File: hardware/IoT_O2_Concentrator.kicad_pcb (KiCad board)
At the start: 2 copper layers, 92.8 x 88.4 mm, 17 parts, among them J1 5V_SUPPLY_BUCK_OUT, J10 12V_SUPPLY_BUCK_IN, J11 O2_VCC_SELECTOR, J12 BOX_SWITCH, J13 AC-DC_MODULE, J2 BUZZER, J3 O2_SENSOR, J4 GPIOs, J5 RELAY, J6 LCD_20x04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

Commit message: Finishing the routing
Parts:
- added JP1: 5V_JUMPER, PCM_Jumper_AKL:Jumper_P7.62mm_D1.2mm, F.Cu at (122.7, 88.2)
- added JP2: GND_JUMPER, PCM_Jumper_AKL:Jumper_P7.62mm_D1.2mm, F.Cu at (124.5, 108.1)
- added JP3: 5V_JUMPER, PCM_Jumper_AKL:Jumper_P10.16mm_D1.2mm, F.Cu at (133.3, 70.5)
- added JP4: 5V_JUMPER, PCM_Jumper_AKL:Jumper_P5.08mm_D1.2mm, F.Cu at (125.0, 69.5)
- moved J9 17.2 mm to (178.2, 92.0)
- moved J2 13.4 mm to (178.6, 69.2), turned to -90 degrees
- moved J5 7.85 mm to (178.2, 58.0), turned to 90 degrees
- moved C1 4.99 mm to (177.8, 111.2)
- moved J4 4.98 mm to (178.6, 80.7)
- moved C2 3.52 mm to (160.6, 112.9)
- moved J1 3.10 mm to (178.4, 100.8)
- moved C3 2.88 mm to (119.2, 81.3)
- moved J10 2.85 mm to (146.8, 114.4)
- moved J13 2.48 mm to (126.3, 113.8)
- moved J6 1.05 mm to (133.4, 75.6)
- moved J3 0.60 mm to (121.2, 61.4)
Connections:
- J4 pad 2: /GPIO32 -> /GPIO33
- J4 pad 3: /GPIO33 -> /GPIO32
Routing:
- net /5V_VCC: track 0.00 -> 191.7 mm
- net /SCL_22: track 0.00 -> 91.6 mm
- net /12V_VCC: track 0.00 -> 82.4 mm
- net /3V3_VCC: track 0.00 -> 82.3 mm
- net /POT_34: track 0.00 -> 60.6 mm
- net /O2_RXD: track 0.00 -> 25.2 mm
- net /O2_TXD: track 0.00 -> 25.2 mm
- net /SIM_TXD: track 0.00 -> 20.4 mm
- net /SIM_RXD: track 0.00 -> 16.8 mm
- net GND: track 0.00 -> 13.3 mm
- net /GPIO25: track 0.00 -> 12.8 mm
- net /GPIO32: track 0.00 -> 12.8 mm
- net /GPIO33: track 0.00 -> 12.8 mm
- net /GPIO35: track 0.00 -> 12.7 mm
- net /SDA_21: track 0.00 -> 12.5 mm
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- added copper zone on B.Cu, net GND
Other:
- board size 92.8 x 88.4 mm -> 73.6 x 82 mm

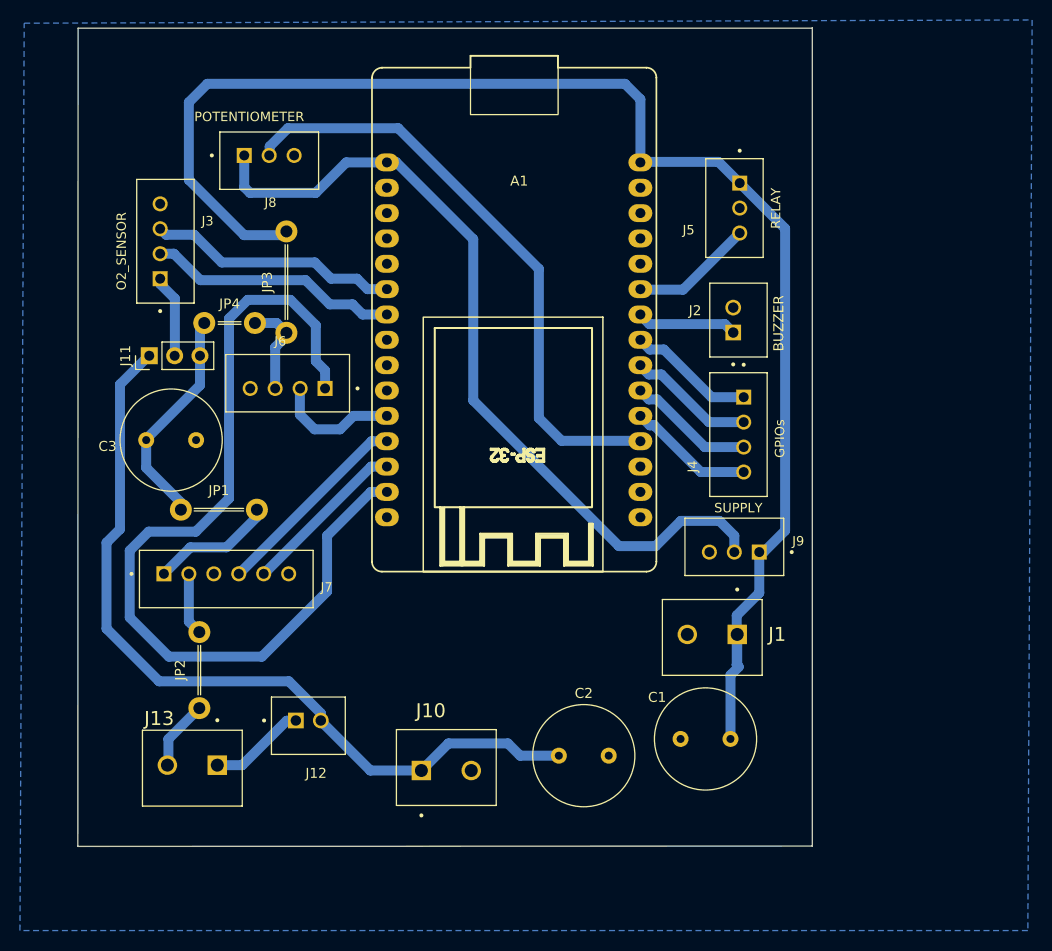
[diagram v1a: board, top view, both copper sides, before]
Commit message: Routing with correct SIM tx/rx & labelling
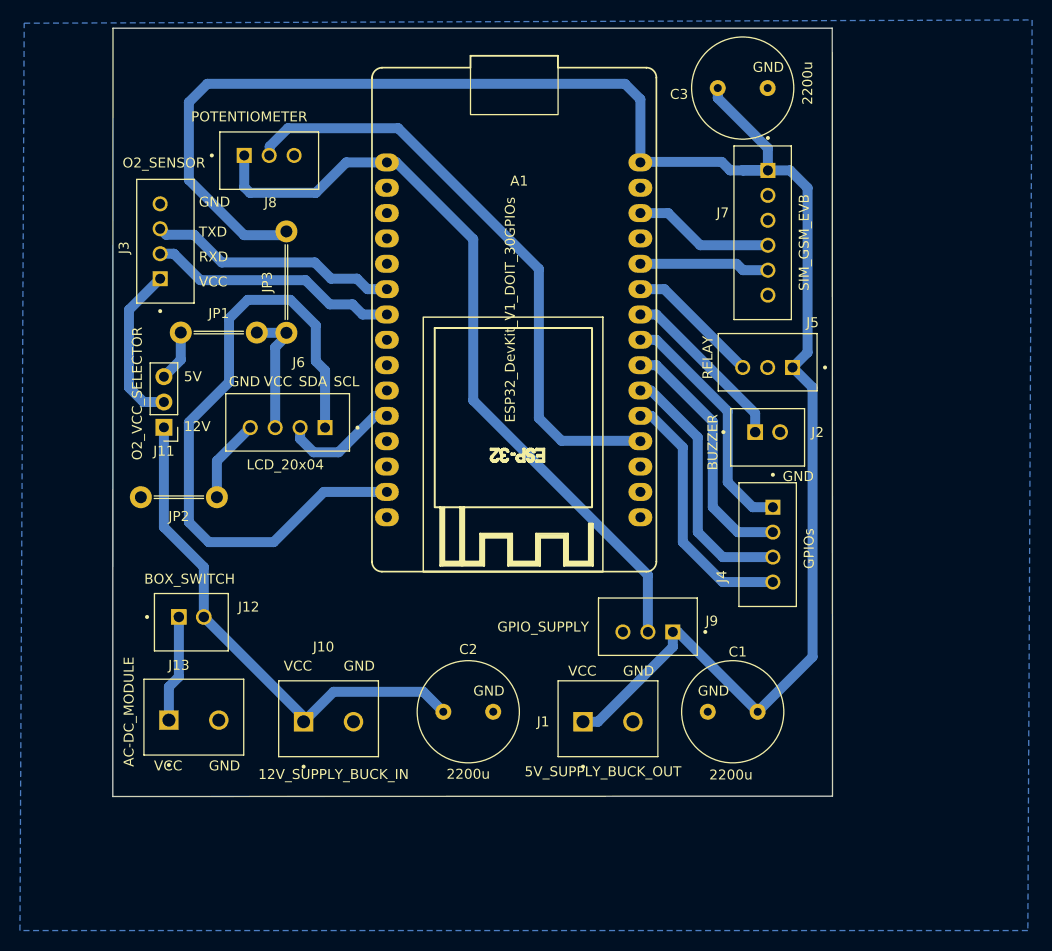
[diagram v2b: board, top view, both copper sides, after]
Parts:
- removed JP4: 5V_JUMPER, PCM_Jumper_AKL:Jumper_P5.08mm_D1.2mm
- J9: value SUPPLY -> GPIO_SUPPLY
- moved C3 67.3 mm to (176.5, 46.0)
- moved J7 64.0 mm to (181.0, 60.5), turned to 90 degrees
- moved JP2 21.2 mm to (126.3, 87.0), turned to 180 degrees
- moved J1 17.8 mm to (163.0, 109.5), turned to 0 degrees
- moved JP1 17.8 mm to (122.7, 70.5)
- moved J5 15.8 mm to (181.5, 73.5), turned to 0 degrees
- moved J12 15.7 mm to (123.8, 99.5)
- moved J10 12.8 mm to (135.0, 109.5)
- moved C2 12.4 mm to (149.0, 108.5)
- moved J2 12.1 mm to (181.5, 81.0), turned to 180 degrees
- moved J9 11.8 mm to (169.5, 100.0)
- moved J4 11.4 mm to (181.5, 91.8)
- moved J11 7.32 mm to (121.0, 80.0), turned to 180 degrees
- moved J13 6.62 mm to (121.5, 109.3), turned to 0 degrees
- moved J6 3.92 mm to (133.4, 79.5)
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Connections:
- A1 pad 12: /SIM_TXD -> unconnected-(A1-RX0/GPIO3-Pad12)
- A1 pad 13: /SIM_RXD -> unconnected-(A1-TX0/GPIO1-Pad13)
- A1 pad 26: unconnected-(A1-ADC2_CH6/D14-Pad26) -> /SIM_RXD
- A1 pad 28: unconnected-(A1-ADC2_CH4/D13-Pad28) -> /SIM_TXD
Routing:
- net /12V_VCC: track 82.4 -> 51.4 mm
- net /SCL_22: track 91.6 -> 66.0 mm
- net /GPIO35: track 12.7 -> 25.7 mm
- net /GPIO32: track 12.8 -> 25.8 mm
- net /GPIO33: track 12.8 -> 25.2 mm
- net /5V_VCC: track 191.7 -> 203.5 mm
- net /GPIO25: track 12.8 -> 24.4 mm
- net /O2_VCC: track 8.31 -> 16.3 mm
- net /BUZZER_26: track 10.1 -> 17.5 mm
- net /SIM_TXD: track 20.4 -> 14.1 mm
- net /3V3_VCC: track 82.3 -> 77.3 mm
- net GND: track 13.3 -> 8.36 mm
- net /SIM_RXD: track 16.8 -> 13.0 mm
- net /RELAY_27: track 12.4 -> 13.5 mm
- net /12V_RAW: track 9.69 -> 10.8 mm
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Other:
- board size 73.6 x 82 mm -> 72.1 x 77 mm
- board text added: "12V"
- board text added: "5V"
- board text added: "GND"
- board text added: "RXD"
- board text added: "SCL"
- board text added: "SDA"
- board text added: "TXD"
- board text added: "VCC"

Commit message: PCB Routing completed
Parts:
- A1: value ESP32_DevKit_V1_DOIT_30GPIOs -> ESP32_DevKit
- C1, C2, C3: footprint Capacitor_THT:C_Radial_D10.0mm_H20.0mm_P5.00mm -> Capacitor_THT:C_Radial_D10.0mm_H12.5mm_P5.00mm
- J1: value 5V_SUPPLY_BUCK_OUT -> 5V_BUCK_OUT
- J10: value 12V_SUPPLY_BUCK_IN -> 12V_BUCK_IN
- J11: value O2_VCC_SELECTOR -> O2_VCC_SEL
- J13: value AC-DC_MODULE -> DC_MODULE
- moved C1 6.98 mm to (173.6, 109.1), turned to 0 degrees
- moved J4 4.90 mm to (181.4, 96.7)
- moved J2 3.53 mm to (181.4, 84.5)
- moved J1 2.60 mm to (160.4, 109.5)
- moved A1 1.96 mm to (142.7, 51.6)
- moved C2 1.43 mm to (147.6, 108.8)
- moved J13 0.16 mm to (121.5, 109.5)
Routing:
- net /12V_VCC: track 51.4 -> 79.4 mm
- net /5V_VCC: track 203.5 -> 225.0 mm
- net /GPIO25: track 24.4 -> 29.9 mm
- net /BUZZER_26: track 17.5 -> 22.8 mm
- net /GPIO35: track 25.7 -> 30.9 mm
- net /GPIO33: track 25.2 -> 30.1 mm
- net /GPIO32: track 25.8 -> 30.4 mm
- net /RELAY_27: track 13.5 -> 16.4 mm
- net /3V3_VCC: track 77.3 -> 80.1 mm
- net /SDA_21: track 11.9 -> 13.9 mm
- net /SIM_TXD: track 14.1 -> 15.5 mm
- net /SIM_RXD: track 13.0 -> 14.4 mm
- net /O2_TXD: track 25.2 -> 24.5 mm
- net /POT_34: track 60.6 -> 59.8 mm
- net /O2_RXD: track 25.2 -> 24.6 mm
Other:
- board text added: "25"
- board text added: "32"
- board text added: "33"
- board text added: "35"
- board text added: "3V3"
- board text added: "IN"
- board text added: "NC"
